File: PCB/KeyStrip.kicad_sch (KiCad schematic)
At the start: 20 parts, among them J1 JST_08, J2 JST_08

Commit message: Fixed a footprint and yeah thats it
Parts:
- removed J1: JST_08, Connector_JST:JST_EH_B8B-EH-A_1x08_P2.50mm_Vertical, symbol PCM_SL_Connectors:JST_08
- D1, D2, D3, D7, D8, D9: footprint (none) -> Library:DualDiode
- D10, D11, D12, D4, D5, D6: footprint ScottoKeebs_Components:LED_SK6812MINI -> Library:SK6812Mini-E
- S1, S2, S3, S4, S5, S6: footprint (none) -> Library:Choc_V1V2_1.00u
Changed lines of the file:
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@@
-	(wire
-		(pts
-			(xy 76.2 116.84) (xy 76.2 119.38)
-		)
-		(stroke
-			(width 0)
-			(type default)
-		)
-	)
 	(wire
 		(pts
@@
 	(wire
 		(pts
-			(xy 60.96 106.68) (xy 60.96 119.38)
-		)
-		(stroke
-			(width 0)
-			(type default)
-		)
-	)
-	(wire
-		(pts
 			(xy 123.19 107.95) (xy 123.19 120.65)
 		)
@@
 	(wire
 		(pts
-			(xy 63.5 110.49) (xy 63.5 119.38)
-		)
-		(stroke
-			(width 0)
-			(type default)
-		)
-	)
-	(wire
-		(pts
 			(xy 121.92 107.95) (xy 121.92 109.22)
 		)
@@
 	(wire
 		(pts
-			(xy 90.17 119.38) (xy 78.74 119.38)
-		)
-		(stroke
-			(width 0)
-			(type default)
-		)
-	)
-	(wire
-		(pts
 			(xy 82.55 90.17) (xy 82.55 93.98)
 		)
@@
 	(wire
 		(pts
-			(xy 73.66 105.41) (xy 73.66 119.38)
-		)
-		(stroke
-			(width 0)
-			(type default)
-		)
-	)
-	(wire
-		(pts
 			(xy 82.55 57.15) (xy 72.39 57.15)
 		)
@@
 	(wire
 		(pts
-			(xy 68.58 102.87) (xy 68.58 119.38)
-		)
-		(stroke
-			(width 0)
-			(type default)
-		)
-	)
-	(wire
-		(pts
 			(xy 120.65 91.44) (xy 127 91.44)
 		)
@@
 	(wire
 		(pts
-			(xy 71.12 111.76) (xy 71.12 119.38)
-		)
-		(stroke
-			(width 0)
-			(type default)
-		)
-	)
-	(wire
-		(pts
 			(xy 120.65 74.93) (xy 132.08 74.93)
 		)
@@
 		(pts
 			(xy 53.34 93.98) (xy 53.34 110.49)
-		)
-		(stroke
-			(width 0)
-			(type default)
-		)
-	)
-	(wire
-		(pts
-			(xy 66.04 107.95) (xy 66.04 119.38)
 		)
 		(stroke
@@
 			)
 		)
-		(property "Footprint" ""
+		(property "Footprint" "Library:DualDiode"
 			(at 120.65 71.12 0)
 			(effects
@@
 			)
 		)
-		(property "Footprint" ""
+		(property "Footprint" "Library:Choc_V1V2_1.00u"
 			(at 118.11 81.28 0)
 			(effects
@@
 			)
 		)
-		(property "Footprint" ""
+		(property "Footprint" "Library:Choc_V1V2_1.00u"
 			(at 55.88 63.5 0)
 			(effects
@@
 			)
 		)
-		(property "Footprint" "ScottoKeebs_Components:LED_SK6812MINI"
+		(property "Footprint" "Library:SK6812Mini-E"
 			(at 74.93 83.82 0)
 			(effects
@@
 				(path "/997a2cad-0c53-407f-a2aa-20d51c5ec46f"
 					(reference "D5")
-					(unit 1)
-				)
-			)
-		)
-	)
-	(symbol
-		(lib_id "PCM_SL_Connectors:JST_08")
-		(at 69.85 123.19 270)
-		(unit 1)
-		(exclude_from_sim no)
-		(in_bom yes)
-		(on_board yes)
-		(dnp no)
-		(fields_autoplaced yes)
-		(property "Reference" "J1"
-			(at 69.85 127 90)
-			(effects
-				(font
-					(size 1.27 1.27)
-				)
-			)
-		)
-		(property "Value" "JST_08"
-			(at 69.85 129.54 90)
-			(effects
-				(font
-					(size 1.27 1.27)
-				)
-			)
-		)
-		(property "Footprint" "Connector_JST:JST_EH_B8B-EH-A_1x08_P2.50mm_Vertical"
-			(at 83.82 123.19 0)
-			(effects
-				(font
-					(size 1.27 1.27)
-				)
-				(hide yes)
-			)
-		)
-		(property "Datasheet" ""
-			(at 83.82 123.19 0)
-			(effects
-				(font
-					(size 1.27 1.27)
-				)
-				(hide yes)
-			)
-		)
-		(property "Description" "JST Connector  8 pins"
-			(at 69.85 123.19 0)
-			(effects
-				(font
-					(size 1.27 1.27)
-				)
-				(hide yes)
-			)
-		)
-		(pin "1"
-		)
-		(pin "2"
-		)
-		(pin "3"
-		)
-		(pin "7"
-		)
-		(pin "6"
-		)
-		(pin "5"
-		)
-		(pin "4"
-		)
-		(pin "8"
-		)
-		(instances
-			(project ""
-				(path "/997a2cad-0c53-407f-a2aa-20d51c5ec46f"
-					(reference "J1")
 					(unit 1)
 				)
@@
 			)
 		)
-		(property "Footprint" ""
+		(property "Footprint" "Library:Choc_V1V2_1.00u"
 			(at 118.11 64.77 0)
 			(effects
@@
 			)
 		)
-		(property "Footprint" "ScottoKeebs_Components:LED_SK6812MINI"
+		(property "Footprint" "Library:SK6812Mini-E"
 			(at 74.93 102.87 0)
 			(effects
@@
 			)
 		)
-		(property "Footprint" ""
+		(property "Footprint" "Library:DualDiode"
 			(at 58.42 86.36 0)
 			(effects
@@
 			)
 		)
-		(property "Footprint" "ScottoKeebs_Components:LED_SK6812MINI"
+		(property "Footprint" "Library:SK6812Mini-E"
 			(at 137.16 85.09 0)
 			(effects
@@
 			)
 		)
-		(property "Footprint" "ScottoKeebs_Components:LED_SK6812MINI"
+		(property "Footprint" "Library:SK6812Mini-E"
 			(at 74.93 66.04 0)
 			(effects
@@
 			)
 		)
-		(property "Footprint" ""
+		(property "Footprint" "Library:DualDiode"
 			(at 120.65 87.63 0)
 			(effects
@@
 			)
 		)
-		(property "Footprint" ""
+		(property "Footprint" "Library:Choc_V1V2_1.00u"
 			(at 55.88 80.01 0)
 			(effects
@@
 			)
 		)
-		(property "Footprint" "ScottoKeebs_Components:LED_SK6812MINI"
+		(property "Footprint" "Library:SK6812Mini-E"
 			(at 137.16 104.14 0)
 			(effects
@@
 			)
 		)
-		(property "Footprint" ""
+		(property "Footprint" "Library:Choc_V1V2_1.00u"
 			(at 118.11 97.79 0)
 			(effects
@@
 					(size 1.27 1.27)
 				)
-				(hide yes)
 			)
 		)
@@
 			)
 		)
-		(property "Footprint" ""
+		(property "Footprint" "Library:DualDiode"
 			(at 120.65 104.14 0)
 			(effects
@@
 			)
 		)
-		(property "Footprint" "ScottoKeebs_Components:LED_SK6812MINI"
+		(property "Footprint" "Library:SK6812Mini-E"
 			(at 137.16 67.31 0)
 			(effects
@@
 			)
 		)
-		(property "Footprint" ""
+		(property "Footprint" "Library:Choc_V1V2_1.00u"
 			(at 55.88 96.52 0)
 			(effects
@@
 			)
 		)
-		(property "Footprint" ""
+		(property "Footprint" "Library:DualDiode"
 			(at 58.42 102.87 0)
 			(effects
@@
 			)
 		)
-		(property "Footprint" ""
+		(property "Footprint" "Library:DualDiode"
 			(at 58.42 69.85 0)
 			(effects

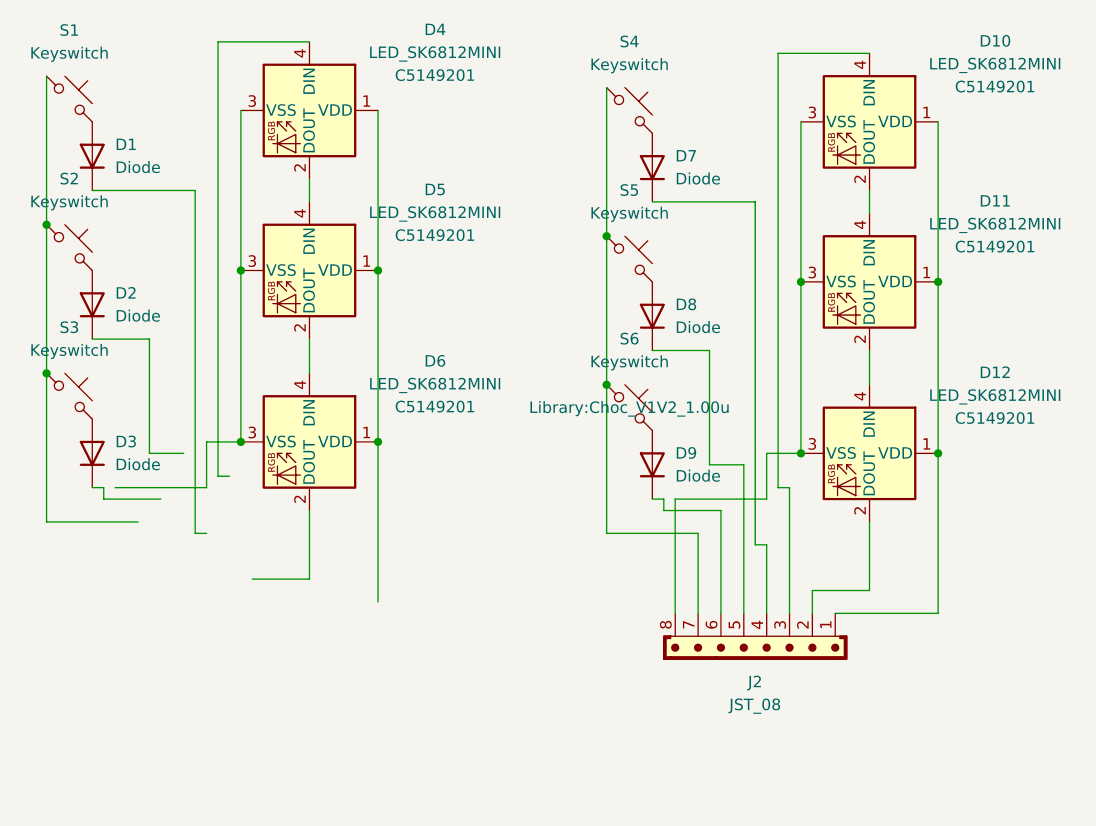
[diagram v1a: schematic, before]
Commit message: Actually well routed and placed this time
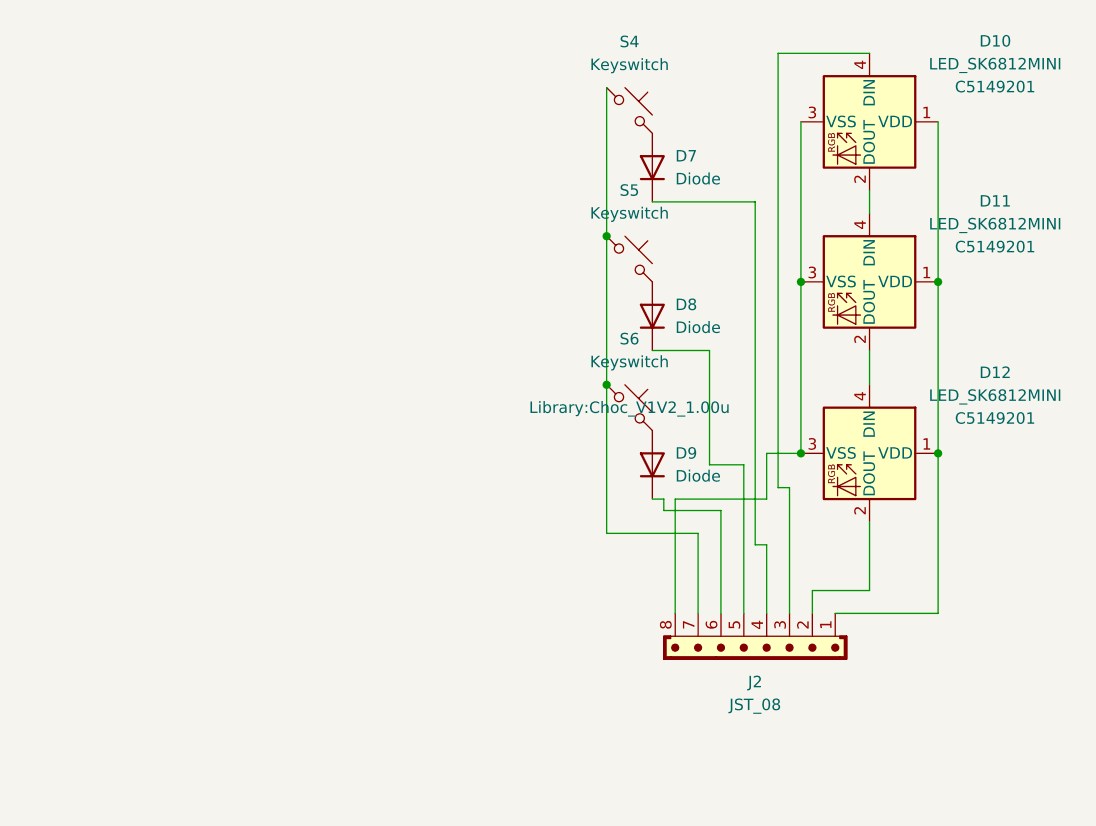
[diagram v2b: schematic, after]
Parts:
- removed D1, D2, D3: Diode, Library:DualDiode, symbol ScottoKeebs:Placeholder_Diode
- removed D4, D5, D6: LED_SK6812MINI, Library:SK6812Mini-E, symbol ScottoKeebs:LED_SK6812MINI
- removed S1, S2, S3: Keyswitch, Library:Choc_V1V2_1.00u, symbol ScottoKeebs:Placeholder_Keyswitch

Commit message: I just gotta add screw holes and solo variations now
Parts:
- J2: footprint Connector_JST:JST_EH_B8B-EH-A_1x08_P2.50mm_Vertical -> Library:JST_EH_B8B-EH-A_1x08_P2.50mm_Vertical
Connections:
- net at D7.1 (K): now also J2.8; no longer J2.4
- net at S4.1, S5.1, S6.1: now also J2.4; no longer J2.7
- net at D10.1 (VDD), D11.1 (VDD), D12.1 (VDD): now also J2.3; no longer J2.1
- net at D10.4 (DIN): now also J2.7; no longer J2.3
- net at J2.5: now also D9.1 (K); no longer D8.1 (K)
- net at J2.6: now also D8.1 (K); no longer D9.1 (K)
- net at D10.3 (VSS), D11.3 (VSS), D12.3 (VSS): now also J2.1; no longer J2.8
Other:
- moved on the sheet: J2
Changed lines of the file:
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@@
+	)
+	(junction
+		(at 152.4 83.82)
+		(diameter 0)
+		(color 0 0 0 0)
+	)
+	(junction
+		(at 115.57 95.25)
+		(diameter 0)
+		(color 0 0 0 0)
+	)
+	(junction
+		(at 115.57 78.74)
+		(diameter 0)
+		(color 0 0 0 0)
 	)
 	(junction
@@
 	)
 	(junction
-		(at 152.4 83.82)
-		(diameter 0)
-		(color 0 0 0 0)
-	)
-	(junction
-		(at 115.57 95.25)
-		(diameter 0)
-		(color 0 0 0 0)
-	)
-	(junction
-		(at 115.57 78.74)
-		(diameter 0)
-		(color 0 0 0 0)
-	)
-	(junction
 		(at 137.16 102.87)
 		(diameter 0)
@@
 	(wire
 		(pts
+			(xy 125.73 120.65) (xy 125.73 130.81)
+		)
+		(stroke
+			(width 0)
+			(type default)
+		)
+	)
+	(wire
+		(pts
 			(xy 115.57 78.74) (xy 115.57 95.25)
 		)
@@
 	(wire
 		(pts
-			(xy 133.35 102.87) (xy 133.35 107.95)
-		)
-		(stroke
-			(width 0)
-			(type default)
-		)
-	)
-	(wire
-		(pts
-			(xy 130.81 104.14) (xy 130.81 120.65)
+			(xy 124.46 105.41) (xy 124.46 125.73)
+		)
+		(stroke
+			(width 0)
+			(type default)
+		)
+	)
+	(wire
+		(pts
+			(xy 110.49 58.42) (xy 110.49 120.65)
 		)
 		(stroke
@@
 	(wire
 		(pts
-			(xy 128.27 109.22) (xy 128.27 120.65)
-		)
-		(stroke
-			(width 0)
-			(type default)
-		)
-	)
-	(wire
-		(pts
-			(xy 132.08 113.03) (xy 133.35 113.03)
-		)
-		(stroke
-			(width 0)
-			(type default)
-		)
-	)
-	(wire
-		(pts
-			(xy 123.19 107.95) (xy 123.19 120.65)
-		)
-		(stroke
-			(width 0)
-			(type default)
-		)
-	)
-	(wire
-		(pts
-			(xy 135.89 106.68) (xy 135.89 120.65)
-		)
-		(stroke
-			(width 0)
-			(type default)
-		)
-	)
-	(wire
-		(pts
-			(xy 134.62 106.68) (xy 135.89 106.68)
-		)
-		(stroke
-			(width 0)
-			(type default)
-		)
-	)
-	(wire
-		(pts
-			(xy 133.35 107.95) (xy 123.19 107.95)
+			(xy 137.16 124.46) (xy 137.16 130.81)
 		)
 		(stroke
@@
 	(wire
 		(pts
+			(xy 127 130.81) (xy 128.27 130.81)
+		)
+		(stroke
+			(width 0)
+			(type default)
+		)
+	)
+	(wire
+		(pts
 			(xy 115.57 95.25) (xy 115.57 111.76)
 		)
@@
 	(wire
 		(pts
-			(xy 115.57 111.76) (xy 125.73 111.76)
+			(xy 138.43 118.11) (xy 138.43 130.81)
 		)
 		(stroke
@@
 	(wire
 		(pts
-			(xy 138.43 118.11) (xy 138.43 120.65)
-		)
-		(stroke
-			(width 0)
-			(type default)
-		)
-	)
-	(wire
-		(pts
-			(xy 152.4 102.87) (xy 152.4 120.65)
+			(xy 137.16 130.81) (xy 135.89 130.81)
+		)
+		(stroke
+			(width 0)
+			(type default)
+		)
+	)
+	(wire
+		(pts
+			(xy 124.46 125.73) (xy 123.19 125.73)
 		)
 		(stroke
@@
 	(wire
 		(pts
+			(xy 132.08 74.93) (xy 132.08 105.41)
+		)
+		(stroke
+			(width 0)
+			(type default)
+		)
+	)
+	(wire
+		(pts
 			(xy 144.78 91.44) (xy 144.78 95.25)
 		)
@@
 	(wire
 		(pts
-			(xy 137.16 102.87) (xy 133.35 102.87)
-		)
-		(stroke
-			(width 0)
-			(type default)
-		)
-	)
-	(wire
-		(pts
-			(xy 121.92 109.22) (xy 128.27 109.22)
-		)
-		(stroke
-			(width 0)
-			(type default)
-		)
-	)
-	(wire
-		(pts
-			(xy 127 104.14) (xy 130.81 104.14)
+			(xy 121.92 109.22) (xy 129.54 109.22)
 		)
 		(stroke
@@
 	(wire
 		(pts
+			(xy 123.19 125.73) (xy 123.19 130.81)
+		)
+		(stroke
+			(width 0)
+			(type default)
+		)
+	)
+	(wire
+		(pts
+			(xy 110.49 58.42) (xy 144.78 58.42)
+		)
+		(stroke
+			(width 0)
+			(type default)
+		)
+	)
+	(wire
+		(pts
+			(xy 137.16 102.87) (xy 137.16 120.65)
+		)
+		(stroke
+			(width 0)
+			(type default)
+		)
+	)
+	(wire
+		(pts
 			(xy 120.65 91.44) (xy 127 91.44)
 		)
@@
 	(wire
 		(pts
-			(xy 144.78 58.42) (xy 134.62 58.42)
-		)
-		(stroke
-			(width 0)
-			(type default)
-		)
-	)
-	(wire
-		(pts
-			(xy 127 91.44) (xy 127 104.14)
+			(xy 137.16 120.65) (xy 140.97 120.65)
+		)
+		(stroke
+			(width 0)
+			(type default)
+		)
+	)
+	(wire
+		(pts
+			(xy 152.4 124.46) (xy 137.16 124.46)
+		)
+		(stroke
+			(width 0)
+			(type default)
+		)
+	)
+	(wire
+		(pts
+			(xy 152.4 102.87) (xy 152.4 124.46)
+		)
+		(stroke
+			(width 0)
+			(type default)
+		)
+	)
+	(wire
+		(pts
+			(xy 132.08 105.41) (xy 124.46 105.41)
+		)
+		(stroke
+			(width 0)
+			(type default)
+		)
+	)
+	(wire
+		(pts
+			(xy 127 91.44) (xy 127 130.81)
 		)
 		(stroke
@@
 	(wire
 		(pts
-			(xy 152.4 120.65) (xy 140.97 120.65)
-		)
-		(stroke
-			(width 0)
-			(type default)
-		)
-	)
-	(wire
-		(pts
-			(xy 133.35 113.03) (xy 133.35 120.65)
-		)
-		(stroke
-			(width 0)
-			(type default)
-		)
-	)
-	(wire
-		(pts
-			(xy 125.73 111.76) (xy 125.73 120.65)
+			(xy 133.35 111.76) (xy 133.35 130.81)
+		)
+		(stroke
+			(width 0)
+			(type default)
+		)
+	)
+	(wire
+		(pts
+			(xy 115.57 111.76) (xy 133.35 111.76)
+		)
+		(stroke
+			(width 0)
+			(type default)
+		)
+	)
+	(wire
+		(pts
+			(xy 140.97 120.65) (xy 140.97 130.81)
+		)
+		(stroke
+			(width 0)
+			(type default)
+		)
+	)
+	(wire
+		(pts
+			(xy 129.54 109.22) (xy 129.54 130.81)
 		)
 		(stroke
@@
 	(wire
 		(pts
-			(xy 134.62 58.42) (xy 134.62 106.68)
-		)
-		(stroke
-			(width 0)
-			(type default)
-		)
-	)
-	(wire
-		(pts
-			(xy 132.08 74.93) (xy 132.08 113.03)
+			(xy 129.54 130.81) (xy 130.81 130.81)
+		)
+		(stroke
+			(width 0)
+			(type default)
+		)
+	)
+	(wire
+		(pts
+			(xy 110.49 120.65) (xy 125.73 120.65)
 		)
 		(stroke
@@
 	(symbol
 		(lib_id "PCM_SL_Connectors:JST_08")
-		(at 132.08 124.46 270)
+		(at 132.08 134.62 270)
 		(unit 1)
 		(exclude_from_sim no)
@@
 		(fields_autoplaced yes)
 		(property "Reference" "J2"
-			(at 132.08 128.27 90)
+			(at 132.08 138.43 90)
 			(effects
 				(font
@@
 		)
 		(property "Value" "JST_08"
-			(at 132.08 130.81 90)
-			(effects
-				(font
-					(size 1.27 1.27)
-				)
-			)
-		)
-		(property "Footprint" "Connector_JST:JST_EH_B8B-EH-A_1x08_P2.50mm_Vertical"
-			(at 146.05 124.46 0)
+			(at 132.08 140.97 90)
+			(effects
+				(font
+					(size 1.27 1.27)
+				)
+			)
+		)
+		(property "Footprint" "Library:JST_EH_B8B-EH-A_1x08_P2.50mm_Vertical"
+			(at 146.05 134.62 0)
 			(effects
 				(font
@@
 		)
 		(property "Datasheet" ""
-			(at 146.05 124.46 0)
+			(at 146.05 134.62 0)
 			(effects
 				(font
@@
 		)
 		(property "Description" "JST Connector  8 pins"
-			(at 132.08 124.46 0)
-			(effects
-				(font
+			(at 132.08 134.62 0)
+			(effects
+				(font
